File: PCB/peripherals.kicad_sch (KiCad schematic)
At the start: 19 parts, among them J2 Conn_01x02_Pin, J3 Conn_01x02_Pin, J4 Conn_01x03_Pin, J5 Conn_01x03_Pin, J6 Conn_01x03_Pin, J7 Conn_01x07_Pin, J8 Conn_01x08_Socket, J9 Conn_01x02_Pin, U2 MPU-6050

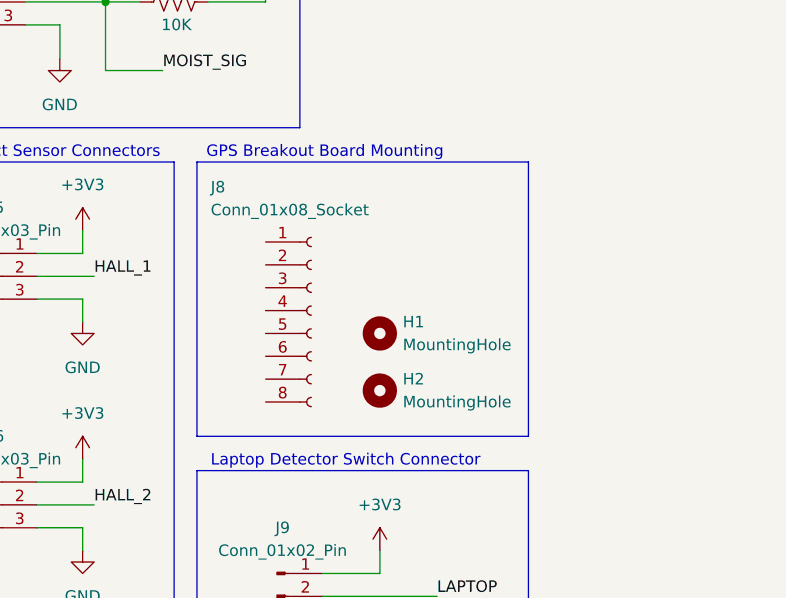
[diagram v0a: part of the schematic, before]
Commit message: add RTC and TX/RX signals
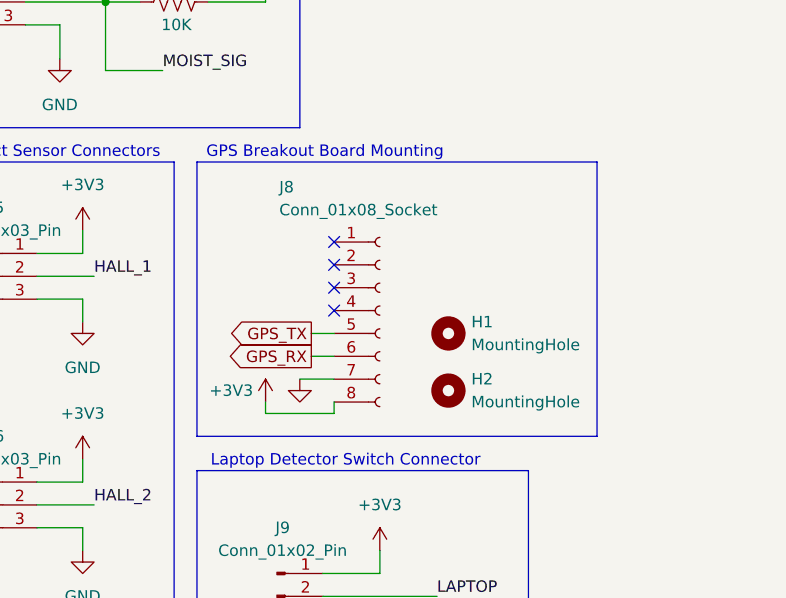
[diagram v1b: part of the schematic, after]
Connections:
- net +3V3: now also J8.8 (Pin_8)
- net GND: now also J8.7 (Pin_7)
- net GPS_TX: now reaches J8.5 (Pin_5)
- net GPS_RX: now reaches J8.6 (Pin_6)
- no-connect marks 5 -> 9
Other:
- moved on the sheet: H1, H2, J8

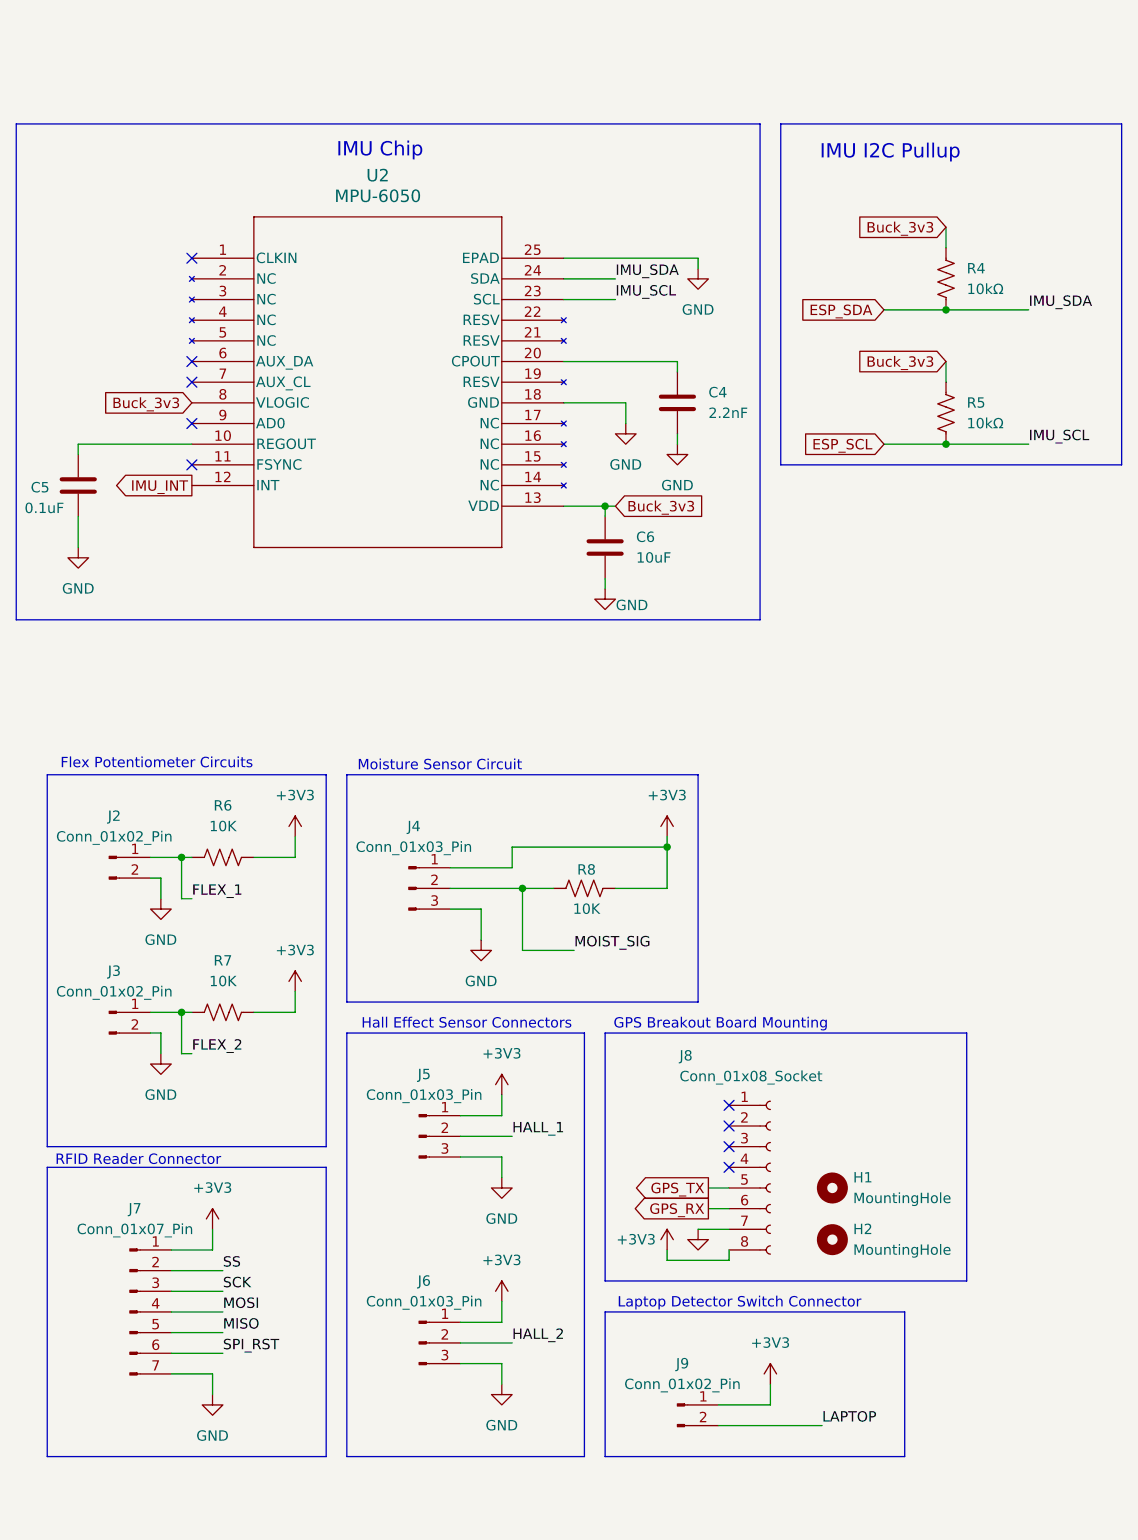
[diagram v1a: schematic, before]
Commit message: add power indicator LEDs, connect peripherals
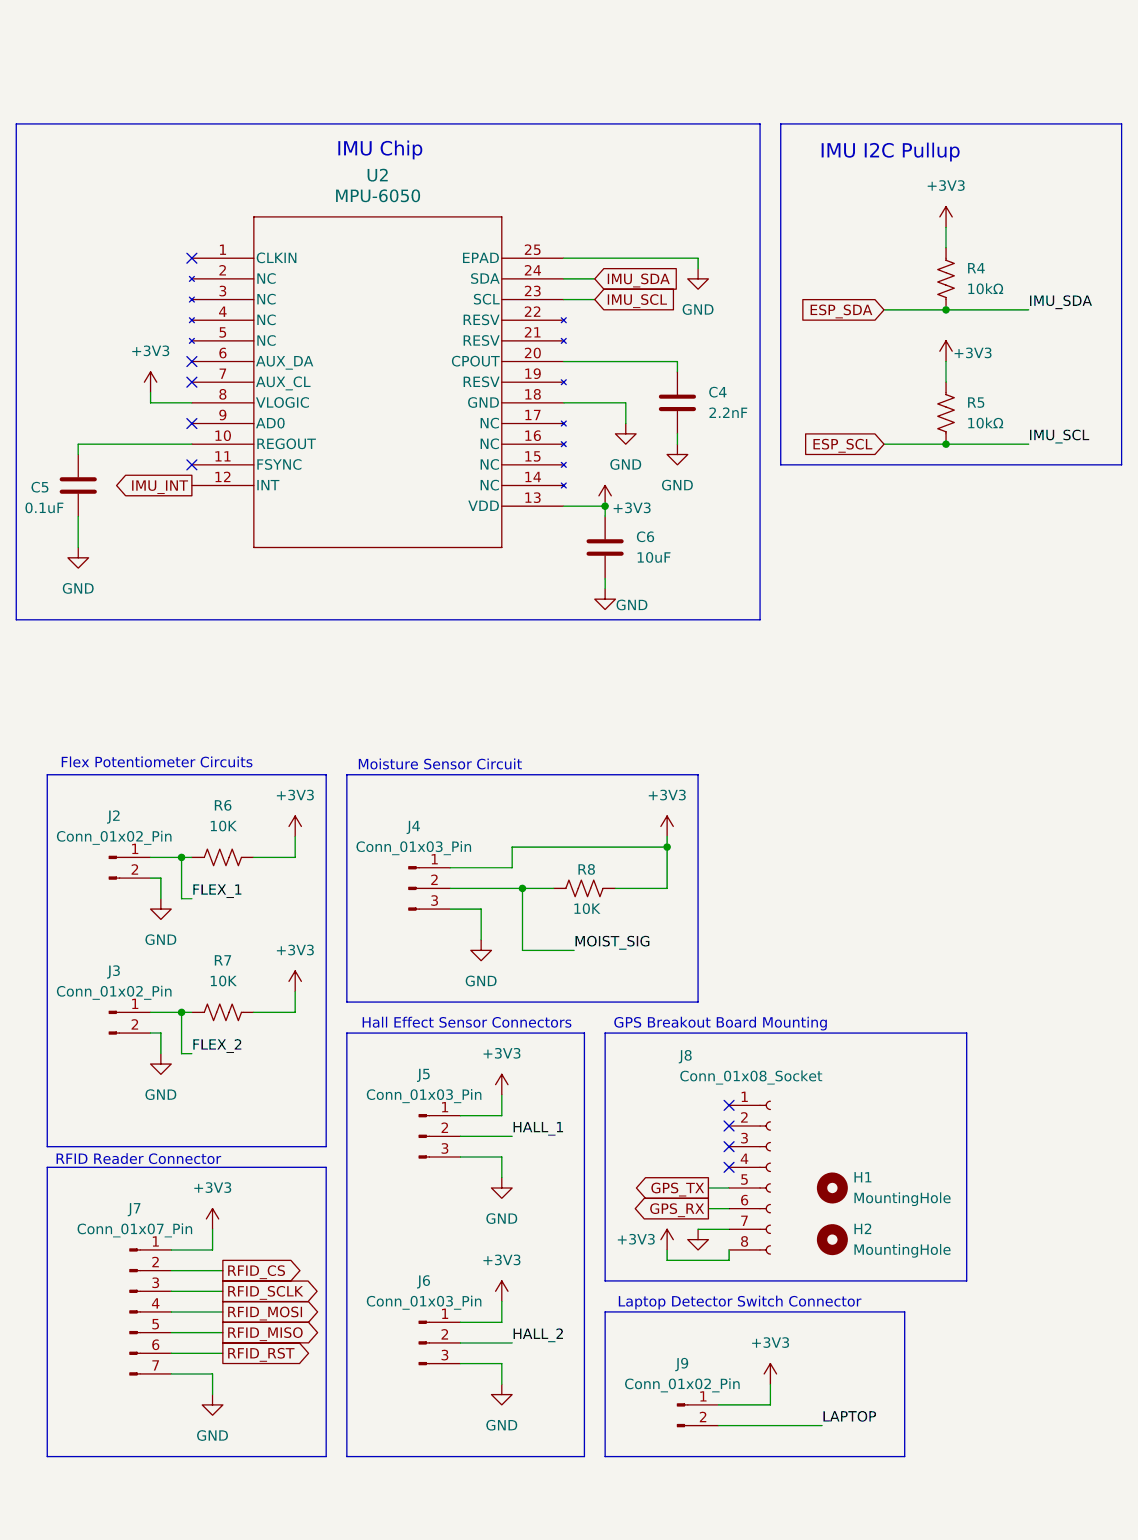
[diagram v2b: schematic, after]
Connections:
- net Buck_3v3 is gone; now on net +3V3: C6.1, R4.1, R5.1, U2.13 (VDD), U2.8 (VLOGIC)
- net MISO renamed RFID_MISO
- net MOSI renamed RFID_MOSI
- net SCK renamed RFID_SCLK
- net SPI_RST renamed RFID_RST
- net SS renamed RFID_CS

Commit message: lots of 'final' schematic updates. ERC is essentially clean, PCB design can begin
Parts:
- removed J9: Conn_01x02_Pin, Connector_JST:JST_VH_B2P-VH_1x02_P3.96mm_Vertical, symbol Connector:Conn_01x02_Pin
- added J1: Conn_01x03_Pin, Connector_JST:JST_VH_B3P-VH_1x03_P3.96mm_Vertical, symbol Connector:Conn_01x03_Pin
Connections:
- net +3V3: now also J1.1 (Pin_1)
- net GND: now also J1.3 (Pin_3)
- net LAPTOP: now also J1.2 (Pin_2)
- net ESP_SCL renamed IMU_SCL
- net ESP_SDA renamed IMU_SDA
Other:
- moved on the sheet: R4, R5

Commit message: place and route connectors, add edges
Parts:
- J1, J4, J5, J6: footprint Connector_JST:JST_VH_B3P-VH_1x03_P3.96mm_Vertical -> Connector_JST:JST_VH_B3PS-VH_1x03_P3.96mm_Horizontal
- J2, J3: footprint Connector_JST:JST_VH_B2P-VH_1x02_P3.96mm_Vertical -> Connector_JST:JST_VH_B2PS-VH_1x02_P3.96mm_Horizontal
- J7: footprint Connector_JST:JST_VH_B7P-VH_1x07_P3.96mm_Vertical -> Connector_JST:JST_VH_B7PS-VH_1x07_P3.96mm_Horizontal
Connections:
- net RFID_CS: now also J7.6 (Pin_6); no longer J7.2 (Pin_2)
- net RFID_MISO: now also J7.4 (Pin_4); no longer J7.5 (Pin_5)
- net RFID_MOSI: now also J7.5 (Pin_5); no longer J7.4 (Pin_4)
- net RFID_RST: now also J7.2 (Pin_2); no longer J7.6 (Pin_6)
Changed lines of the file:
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@@
 	(global_label "RFID_RST"
 		(shape input)
-		(at 39.37 165.1 0)
+		(at 39.37 154.94 0)
 		(fields_autoplaced yes)
 		(effects
@@
 		)
 		(property "Intersheetrefs" "${INTERSHEET_REFS}"
-			(at 51.0033 165.1 0)
+			(at 50.0357 154.94 0)
 			(effects
 				(font
@@
 	(global_label "RFID_MISO"
 		(shape output)
-		(at 39.37 162.56 0)
+		(at 39.37 160.02 0)
 		(fields_autoplaced yes)
 		(effects
@@
 		)
 		(property "Intersheetrefs" "${INTERSHEET_REFS}"
-			(at 52.1524 162.56 0)
+			(at 52.1524 160.02 0)
 			(effects
 				(font
@@
 	(global_label "RFID_MOSI"
 		(shape input)
-		(at 39.37 160.02 0)
+		(at 39.37 162.56 0)
 		(fields_autoplaced yes)
 		(effects
@@
 		)
 		(property "Intersheetrefs" "${INTERSHEET_REFS}"
-			(at 52.1524 160.02 0)
+			(at 52.1524 162.56 0)
 			(effects
 				(font
@@
 	(global_label "RFID_CS"
 		(shape input)
-		(at 39.37 154.94 0)
+		(at 39.37 165.1 0)
 		(fields_autoplaced yes)
 		(effects
@@
 		)
 		(property "Intersheetrefs" "${INTERSHEET_REFS}"
-			(at 50.0357 154.94 0)
+			(at 51.0033 165.1 0)
 			(effects
 				(font
@@
 			)
 		)
-		(property "Footprint" "Connector_JST:JST_VH_B3P-VH_1x03_P3.96mm_Vertical"
+		(property "Footprint" "Connector_JST:JST_VH_B3PS-VH_1x03_P3.96mm_Horizontal"
 			(at 95.25 173.99 0)
 			(effects
@@
 			)
 		)
-		(property "Footprint" "Connector_JST:JST_VH_B2P-VH_1x02_P3.96mm_Vertical"
+		(property "Footprint" "Connector_JST:JST_VH_B2PS-VH_1x02_P3.96mm_Horizontal"
 			(at 25.4 104.14 0)
 			(effects
@@
 			)
 		)
-		(property "Footprint" "Connector_JST:JST_VH_B2P-VH_1x02_P3.96mm_Vertical"
+		(property "Footprint" "Connector_JST:JST_VH_B2PS-VH_1x02_P3.96mm_Horizontal"
 			(at 25.4 123.19 0)
 			(effects
@@
 			)
 		)
-		(property "Footprint" "Connector_JST:JST_VH_B7P-VH_1x07_P3.96mm_Vertical"
+		(property "Footprint" "Connector_JST:JST_VH_B7PS-VH_1x07_P3.96mm_Horizontal"
 			(at 27.94 160.02 0)
 			(effects
@@
 			)
 		)
-		(property "Footprint" "Connector_JST:JST_VH_B3P-VH_1x03_P3.96mm_Vertical"
+		(property "Footprint" "Connector_JST:JST_VH_B3PS-VH_1x03_P3.96mm_Horizontal"
 			(at 63.5 138.43 0)
 			(effects
@@
 			)
 		)
-		(property "Footprint" "Connector_JST:JST_VH_B3P-VH_1x03_P3.96mm_Vertical"
+		(property "Footprint" "Connector_JST:JST_VH_B3PS-VH_1x03_P3.96mm_Horizontal"
 			(at 63.5 163.83 0)
 			(effects
@@
 			)
 		)
-		(property "Footprint" "Connector_JST:JST_VH_B3P-VH_1x03_P3.96mm_Vertical"
+		(property "Footprint" "Connector_JST:JST_VH_B3PS-VH_1x03_P3.96mm_Horizontal"
 			(at 62.23 107.95 0)
 			(effects

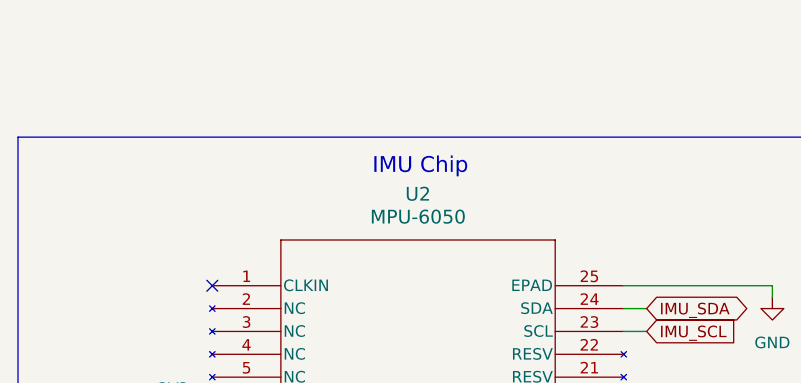
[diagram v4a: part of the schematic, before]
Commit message: Some updates suggested by Ryan (The 1 sem senior design prof)
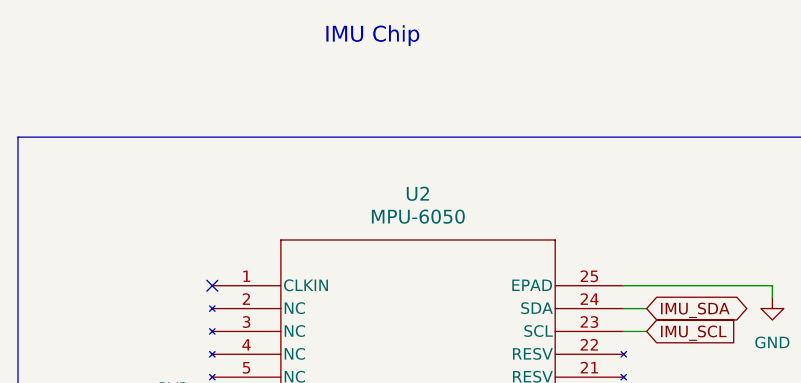
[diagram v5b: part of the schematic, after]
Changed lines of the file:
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@@
 	(text "IMU Chip"
 		(exclude_from_sim no)
-		(at 58.674 17.272 0)
+		(at 53.34 2.794 0)
 		(effects
 			(font

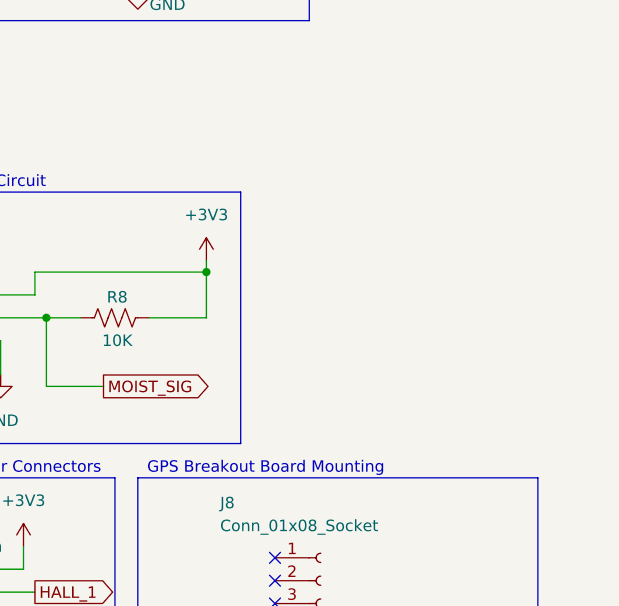
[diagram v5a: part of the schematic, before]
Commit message: Added motors :pensive:
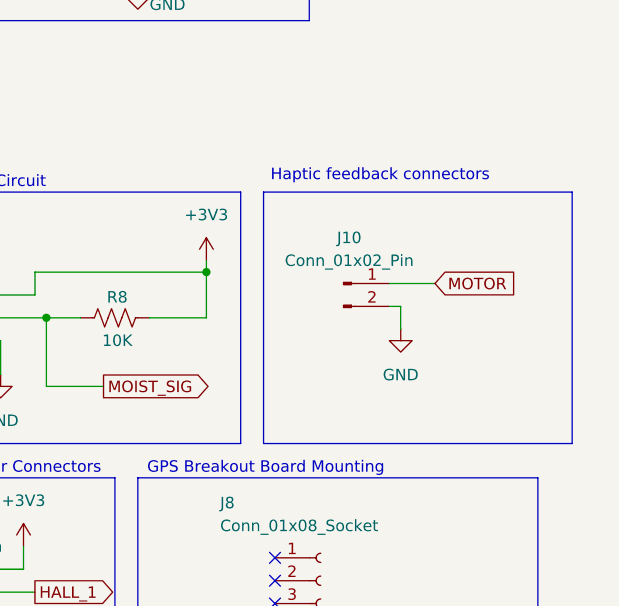
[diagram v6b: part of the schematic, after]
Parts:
- added J10: Conn_01x02_Pin, Connector_JST:JST_VH_B2PS-VH_1x02_P3.96mm_Horizontal, symbol Connector:Conn_01x02_Pin
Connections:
- net GND: now also J10.2 (Pin_2)
- new net MOTOR: J10.1 (Pin_1)
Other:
- note added: "Haptic feedback connectors"
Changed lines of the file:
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@@
 	)
 	(rectangle
+		(start 100.33 93.98)
+		(end 134.62 121.92)
+		(stroke
+			(width 0)
+			(type default)
+		)
+		(fill
+			(type none)
+		)
+	)
+	(rectangle
 		(start 54.61 93.98)
 		(end 97.79 121.92)
@@
 		)
 	)
+	(text "Haptic feedback connectors"
+		(exclude_from_sim no)
+		(at 113.284 92.202 0)
+		(effects
+			(font
+				(size 1.27 1.27)
+			)
+		)
+	)
 	(text "Moisture Sensor Circuit"
 		(exclude_from_sim no)
@@
 	(wire
 		(pts
+			(xy 115.57 106.68) (xy 115.57 109.22)
+		)
+		(stroke
+			(width 0)
+			(type default)
+		)
+	)
+	(wire
+		(pts
 			(xy 21.59 62.23) (xy 21.59 66.04)
 		)
@@
 	(wire
 		(pts
+			(xy 114.3 104.14) (xy 119.38 104.14)
+		)
+		(stroke
+			(width 0)
+			(type default)
+		)
+	)
+	(wire
+		(pts
 			(xy 93.98 152.4) (xy 93.98 153.67)
 		)
@@
 	(wire
 		(pts
+			(xy 114.3 106.68) (xy 115.57 106.68)
+		)
+		(stroke
+			(width 0)
+			(type default)
+		)
+	)
+	(wire
+		(pts
 			(xy 68.58 161.29) (xy 73.66 161.29)
 		)
@@
 		)
 	)
+	(global_label "MOTOR"
+		(shape input)
+		(at 119.38 104.14 0)
+		(fields_autoplaced yes)
+		(effects
+			(font
+				(size 1.27 1.27)
+			)
+			(justify left)
+		)
+		(property "Intersheetrefs" "${INTERSHEET_REFS}"
+			(at 128.7152 104.14 0)
+			(effects
+				(font
+					(size 1.27 1.27)
+				)
+				(justify left)
+				(hide yes)
+			)
+		)
+	)
 	(global_label "RFID_CS"
 		(shape input)
@@
 	(symbol
 		(lib_id "power:GND")
+		(at 115.57 109.22 0)
+		(unit 1)
+		(exclude_from_sim no)
+		(in_bom yes)
+		(on_board yes)
+		(dnp no)
+		(fields_autoplaced yes)
+		(property "Reference" "#PWR054"
+			(at 115.57 115.57 0)
+			(effects
+				(font
+					(size 1.27 1.27)
+				)
+				(hide yes)
+			)
+		)
+		(property "Value" "GND"
+			(at 115.57 114.3 0)
+			(effects
+				(font
+					(size 1.27 1.27)
+				)
+			)
+		)
+		(property "Footprint" ""
+			(at 115.57 109.22 0)
+			(effects
+				(font
+					(size 1.27 1.27)
+				)
+				(hide yes)
+			)
+		)
+		(property "Datasheet" ""
+			(at 115.57 109.22 0)
+			(effects
+				(font
+					(size 1.27 1.27)
+				)
+				(hide yes)
+			)
+		)
+		(property "Description" "Power symbol creates a global label with name \"GND\" , ground"
+			(at 115.57 109.22 0)
+			(effects
+				(font
+					(size 1.27 1.27)
+				)
+				(hide yes)
+			)
+		)
+		(pin "1"
+		)
+		(instances
+			(project "Smart_Backpack"
+				(path "/38abc652-c887-4ef7-a45f-d93ca7f4b2d6/d6ce3c21-a733-4fa1-8134-cea10a02c4e5"
+					(reference "#PWR054")
+					(unit 1)
+				)
+			)
+		)
+	)
+	(symbol
+		(lib_id "power:GND")
 		(at 106.68 179.07 0)
 		(unit 1)
@@
 					(unit 1)
 				)
+			)
+		)
+	)
+	(symbol
+		(lib_id "Connector:Conn_01x02_Pin")
+		(at 109.22 104.14 0)
+		(unit 1)
+		(exclude_from_sim no)
+		(in_bom yes)
+		(on_board yes)
+		(dnp no)
+		(property "Reference" "J10"
+			(at 109.855 99.06 0)
+			(effects
+				(font
+					(size 1.27 1.27)
+				)
+			)
+		)
+		(property "Value" "Conn_01x02_Pin"
+			(at 109.855 101.6 0)
+			(effects
+				(font
+					(size 1.27 1.27)
+				)
+			)
+		)
+		(property "Footprint" "Connector_JST:JST_VH_B2PS-VH_1x02_P3.96mm_Horizontal"
+			(at 109.22 104.14 0)
+			(effects
+				(font
+					(size 1.27 1.27)
+				)
+				(hide yes)
+			)
+		)
+		(property "Datasheet" "~"
+			(at 109.22 104.14 0)
+			(effects
+				(font
+					(size 1.27 1.27)
+				)
+				(hide yes)
+			)
+		)
+		(property "Description" "Generic connector, single row, 01x02, script generated"
+			(at 109.22 104.14 0)
+			(effects
+				(font
+					(size 1.27 1.27)
+				)
+				(hide yes)
+			)
+		)
+		(pin "1"
+		)
+		(pin "2"
+		)
+		(instances
+			(project "Smart_Backpack"
+				(path "/38abc652-c887-4ef7-a45f-d93ca7f4b2d6/d6ce3c21-a733-4fa1-8134-cea10a02c4e5"
+					(reference "J10")
+					(unit 1)
+				)
